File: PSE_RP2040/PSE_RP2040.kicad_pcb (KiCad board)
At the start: 2 copper layers, 100 x 50 mm, 0 parts

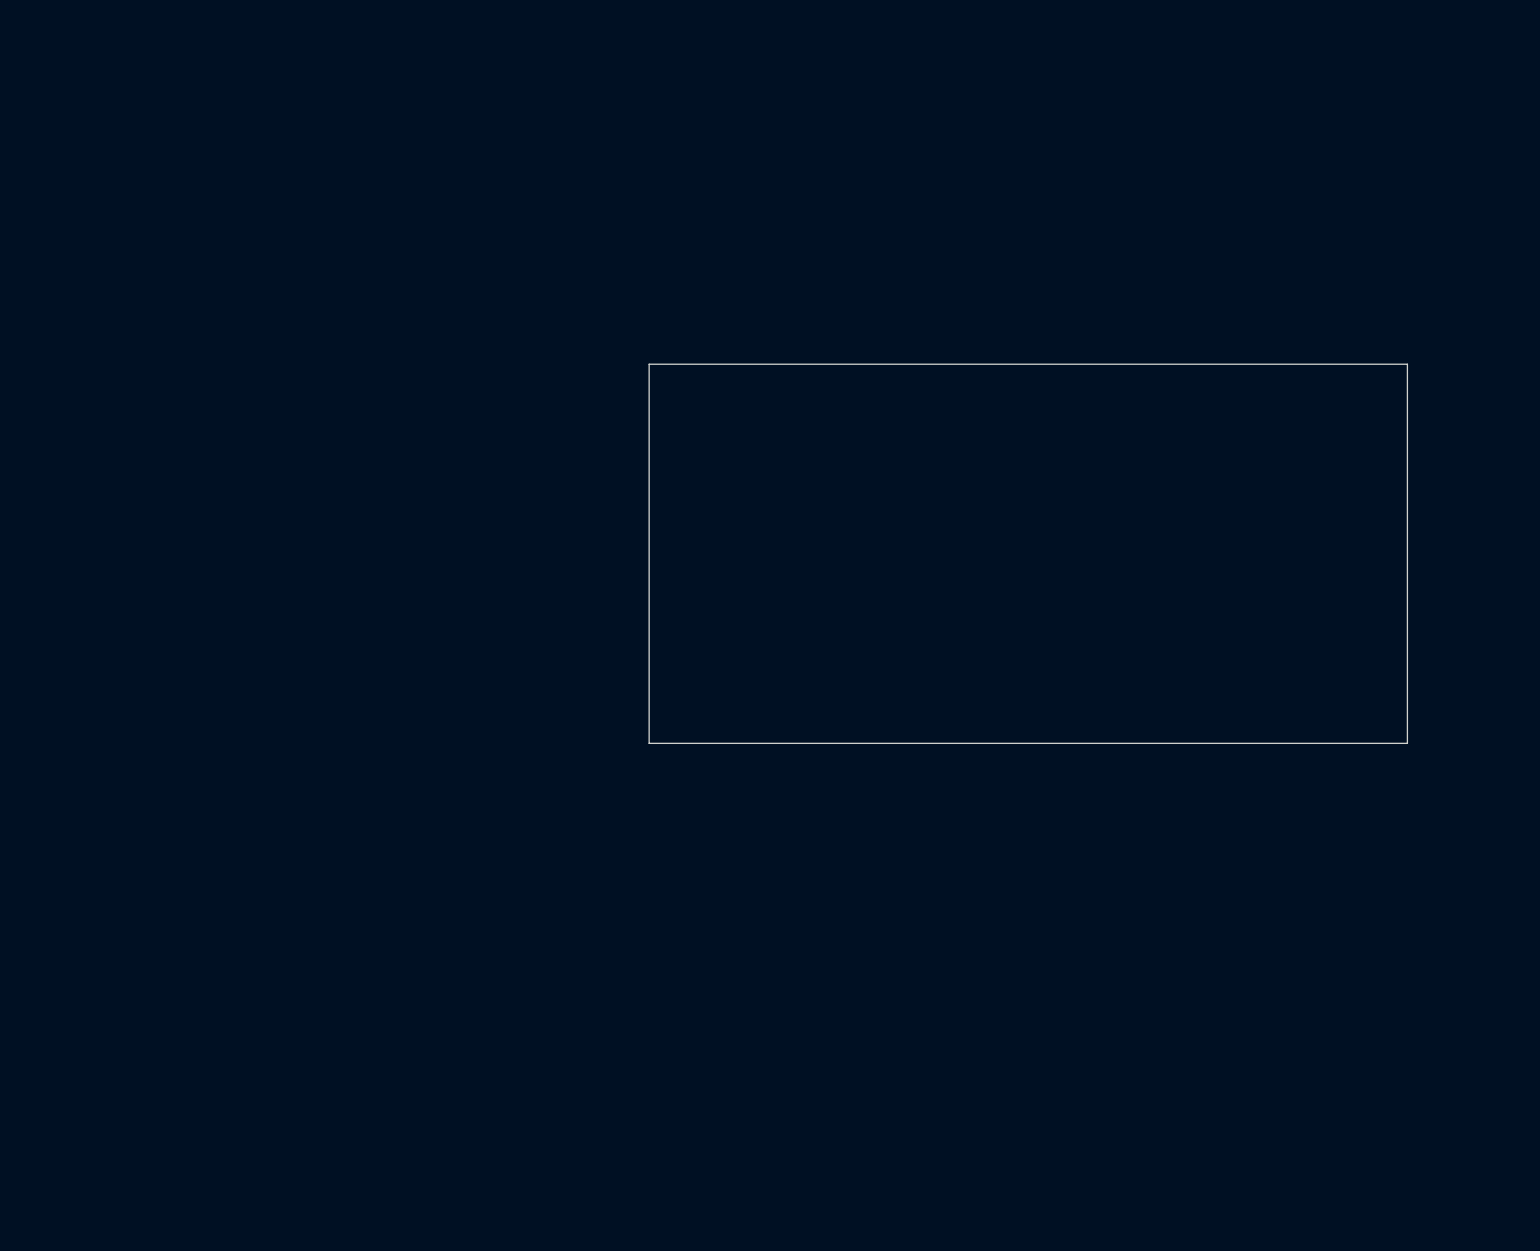
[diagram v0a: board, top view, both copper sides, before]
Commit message: check pin, footprint e symb mem
tolto pin 9 al simbolo memoria
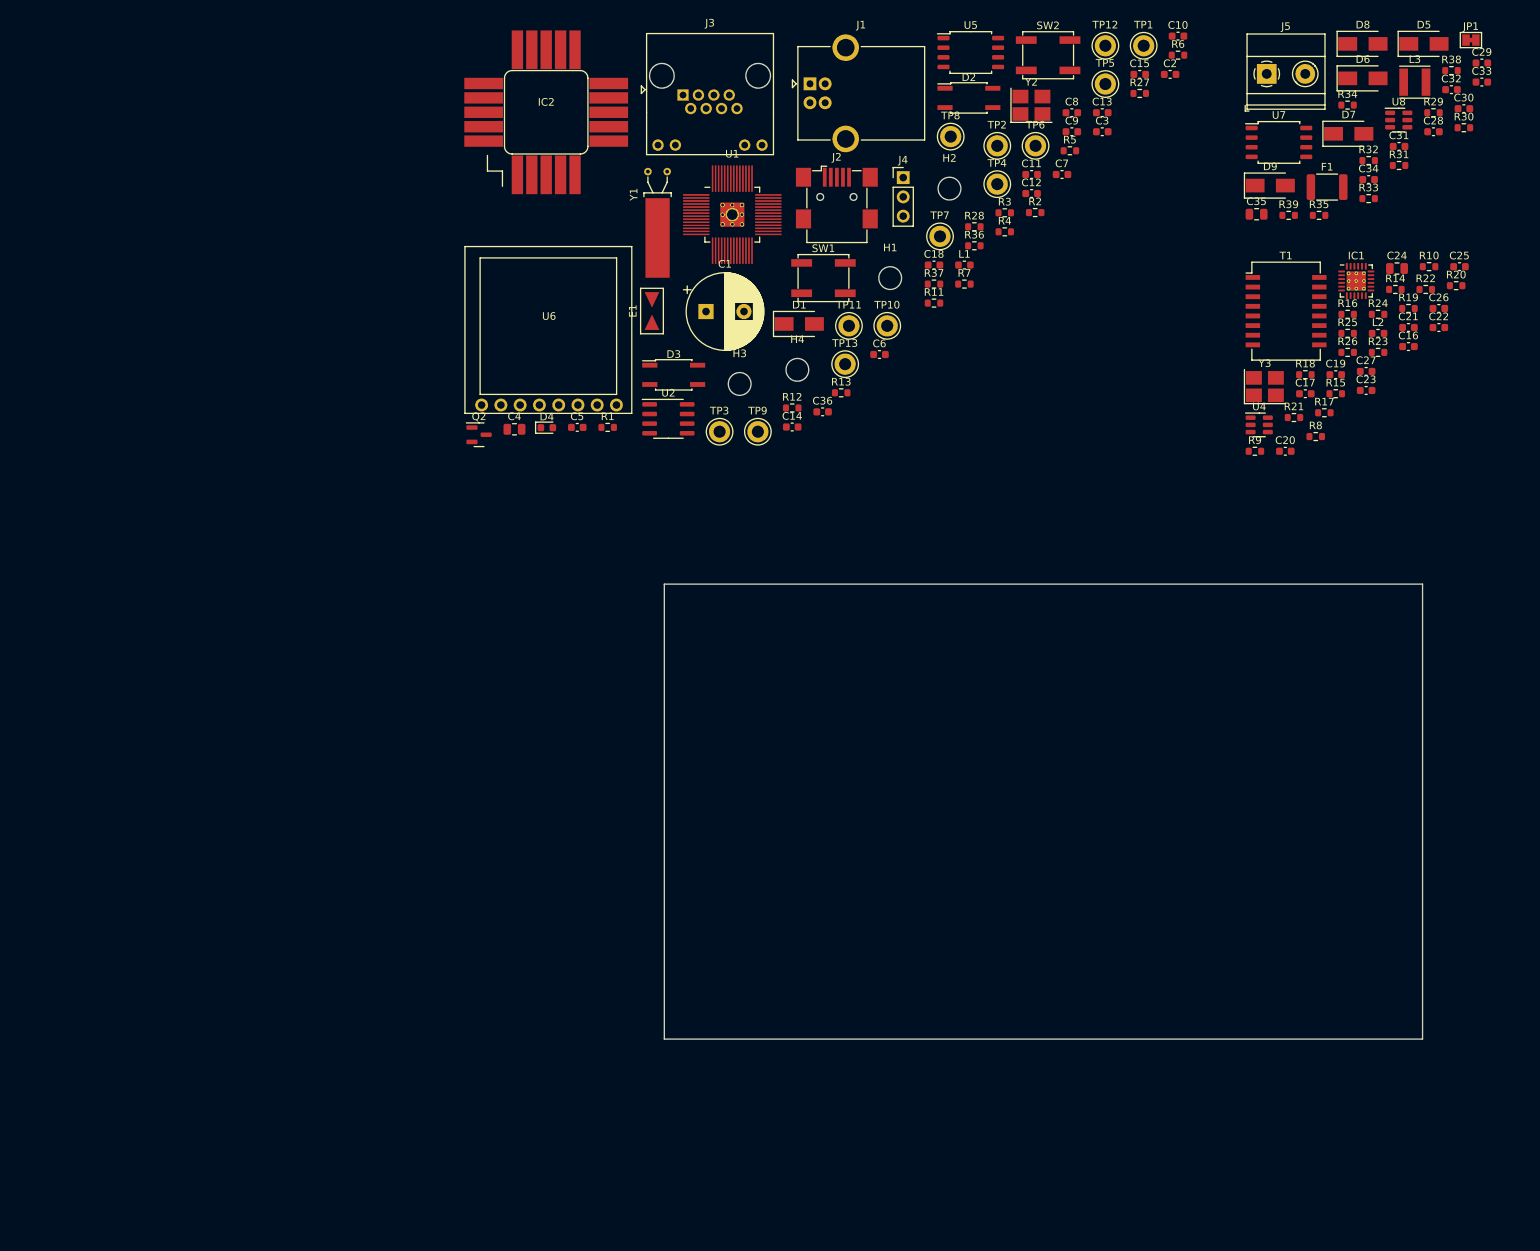
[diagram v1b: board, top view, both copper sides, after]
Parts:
- added C1: 0.1F, Capacitor_THT:CP_Radial_D10.0mm_P5.00mm, F.Cu at (105.5, 64.0)
- added C10: 100n, Capacitor_SMD:C_0603_1608Metric, F.Cu at (167.8, 27.7)
- added C11: 100n, Capacitor_SMD:C_0603_1608Metric, F.Cu at (148.4, 46.0)
- added C12: 2u2, Capacitor_SMD:C_0603_1608Metric, F.Cu at (148.4, 48.5)
- added C13: 100n, Capacitor_SMD:C_0603_1608Metric, F.Cu at (157.8, 37.8)
- added C14: 2u2, Capacitor_SMD:C_0603_1608Metric, F.Cu at (116.9, 79.3)
- added C15: 100n, Capacitor_SMD:C_0603_1608Metric, F.Cu at (162.7, 32.8)
- added C16: 100n, Capacitor_SMD:C_0603_1608Metric, F.Cu at (198.1, 68.7)
- added C17: 1u, Capacitor_SMD:C_0603_1608Metric, F.Cu at (184.5, 74.9)
- added C18: 2u2, Capacitor_SMD:C_0603_1608Metric, F.Cu at (135.6, 57.9)
- added C19: 470p, Capacitor_SMD:C_0603_1608Metric, F.Cu at (188.6, 72.4)
- added C2: 12p, Capacitor_SMD:C_0603_1608Metric, F.Cu at (166.7, 32.8)
- added C20: 12p, Capacitor_SMD:C_0603_1608Metric, F.Cu at (181.9, 82.5)
- added C21: 12p, Capacitor_SMD:C_0603_1608Metric, F.Cu at (198.1, 66.2)
- added C22: 100n, Capacitor_SMD:C_0603_1608Metric, F.Cu at (202.2, 66.2)
- added C23: 100n, Capacitor_SMD:C_0603_1608Metric, F.Cu at (192.6, 74.5)
- added C24: 10u 16V, Capacitor_SMD:C_0805_2012Metric, F.Cu at (196.6, 58.4)
- added C25: 100n, Capacitor_SMD:C_0603_1608Metric, F.Cu at (204.9, 58.1)
- added C26: 100n, Capacitor_SMD:C_0603_1608Metric, F.Cu at (202.2, 63.6)
- added C27: 100n, Capacitor_SMD:C_0603_1608Metric, F.Cu at (192.6, 72.0)
- added C28: 100n 100v, Capacitor_SMD:C_0603_1608Metric, F.Cu at (201.4, 40.3)
- added C29: 2u2, Capacitor_SMD:C_0603_1608Metric, F.Cu at (207.8, 31.3)
- added C3: 100n, Capacitor_SMD:C_0603_1608Metric, F.Cu at (157.8, 40.3)
- added C30: 2u2, Capacitor_SMD:C_0603_1608Metric, F.Cu at (205.4, 37.3)
- added C31: 100n 100v, Capacitor_SMD:C_0603_1608Metric, F.Cu at (196.9, 42.3)
- added C32: 100n, Capacitor_SMD:C_0603_1608Metric, F.Cu at (203.8, 34.8)
- added C33: 470p, Capacitor_SMD:C_0603_1608Metric, F.Cu at (207.8, 33.8)
- added C34: 100n, Capacitor_SMD:C_0603_1608Metric, F.Cu at (192.9, 46.6)
- added C35: 100u, Capacitor_SMD:C_0805_2012Metric, F.Cu at (178.1, 51.2)
- added C36: 10n, Capacitor_SMD:C_0603_1608Metric, F.Cu at (120.9, 77.3)
- added C4: 10u, Capacitor_SMD:C_0805_2012Metric, F.Cu at (80.2, 79.6)
- added C5: 12p, Capacitor_SMD:C_0603_1608Metric, F.Cu at (88.5, 79.3)
- added C6: 100n, Capacitor_SMD:C_0603_1608Metric, F.Cu at (128.4, 69.7)
- added C7: 100n, Capacitor_SMD:C_0603_1608Metric, F.Cu at (152.4, 46.0)
- added C8: 100n, Capacitor_SMD:C_0603_1608Metric, F.Cu at (153.8, 37.8)
- added C9: 100n, Capacitor_SMD:C_0603_1608Metric, F.Cu at (153.8, 40.3)
- added D1: D_Schottky, Diode_SMD:D_SMA, F.Cu at (117.8, 65.7)
- added D2: MB1S, Package_SO:SO-4_4.4x3.6mm_P2.54mm, F.Cu at (140.2, 35.9)
- added D3: MB1S, Package_SO:SO-4_4.4x3.6mm_P2.54mm, F.Cu at (101.2, 72.4)
- added D4: LED, LED_SMD:LED_0603_1608Metric, F.Cu at (84.5, 79.4)
- added D5: S1B, Diode_SMD:D_SMA, F.Cu at (200.2, 28.8)
- added D6: D_Schottky, Diode_SMD:D_SMA, F.Cu at (192.1, 33.3)
- added D7: SMAJ56, Diode_SMD:D_SMA, F.Cu at (190.3, 40.6)
- added D8: S1B, Diode_SMD:D_SMA, F.Cu at (192.1, 28.8)
- added D9: D_Schottky, Diode_SMD:D_SMA, F.Cu at (179.9, 47.4)
- added E1: SparkGap, PSE2021:SPARK_GAP_TRIANGLE, F.Cu at (98.4, 64.0)
- added F1: Polyfuse_Small: fino a 500ma, Fuse:Fuse_1812_4532Metric, F.Cu at (187.4, 47.6)
- added H1: MountingHole, MountingHole:MountingHole_3mm, F.Cu at (129.8, 59.6)
- added H2: MountingHole, MountingHole:MountingHole_3mm, F.Cu at (137.6, 47.8)
- added H3: MountingHole, MountingHole:MountingHole_3mm, F.Cu at (109.9, 73.6)
- added H4: MountingHole, MountingHole:MountingHole_3mm, F.Cu at (117.5, 71.7)
- added IC1: LAN8742A-CZ, Package_DFN_QFN:HVQFN-24-1EP_4x4mm_P0.5mm_EP2.5x2.5mm_ThermalVias, F.Cu at (191.3, 60.0)
- added IC2: SAM-M8Q-0, PSE2021:SAM-M8Q, F.Cu at (84.4, 37.8)
- added J1: USB_B, Connector_USB:USB_B_OST_USB-B1HSxx_Horizontal, F.Cu at (119.2, 34.0)
- added J2: USB_B_Mini, Connector_USB:USB_Mini-B_Wuerth_65100516121_Horizontal, F.Cu at (122.8, 48.9)
- added J3: 8P8C_LED, PSE2021:RJ45_Amphenol_RJHSE-5081, F.Cu at (102.5, 35.5)
- added J4: Conn_01x03, Connector_PinHeader_2.54mm:PinHeader_1x03_P2.54mm_Vertical, F.Cu at (131.5, 46.4)
- added J5: Screw_Terminal_01x02, TerminalBlock_Phoenix:TerminalBlock_Phoenix_MKDS-1,5-2-5.08_1x02_P5.08mm_Horizontal, F.Cu at (179.4, 32.7)
- added JP1: SolderJumper_2_Bridged, Jumper:SolderJumper-2_P1.3mm_Bridged_Pad1.0x1.5mm, F.Cu at (206.4, 28.2)
- added L1: 200mA 120Ohm, Inductor_SMD:L_0603_1608Metric, F.Cu at (139.6, 57.9)
- added L2: 25uH, Inductor_SMD:L_0603_1608Metric, F.Cu at (194.1, 66.9)
- added L3: 22u, Inductor_SMD:L_Vishay_IFSC-1515AH_4x4x1.8mm, F.Cu at (199.0, 33.8)
- added Q2: IRLML6402, Package_TO_SOT_SMD:SOT-23, F.Cu at (75.6, 80.3)
- added R1: 1k, Resistor_SMD:R_0603_1608Metric, F.Cu at (92.5, 79.3)
- added R10: 10k, Resistor_SMD:R_0603_1608Metric, F.Cu at (200.9, 58.1)
- added R11: 1k, Resistor_SMD:R_0603_1608Metric, F.Cu at (135.6, 62.9)
- added R12: 27, Resistor_SMD:R_0603_1608Metric, F.Cu at (116.9, 76.8)
- added R13: 27, Resistor_SMD:R_0603_1608Metric, F.Cu at (123.3, 74.8)
- added R14: 10k, Resistor_SMD:R_0603_1608Metric, F.Cu at (196.4, 61.1)
- added R15: 10k, Resistor_SMD:R_0603_1608Metric, F.Cu at (188.6, 74.9)
- added R16: 33, Resistor_SMD:R_0603_1608Metric, F.Cu at (190.1, 64.4)
- added R17: 10k, Resistor_SMD:R_0603_1608Metric, F.Cu at (187.1, 77.4)
- added R18: 10k, Resistor_SMD:R_0603_1608Metric, F.Cu at (184.5, 72.4)
- added R19: 10k, Resistor_SMD:R_0603_1608Metric, F.Cu at (198.1, 63.6)
- added R2: 100, Resistor_SMD:R_0603_1608Metric, F.Cu at (148.9, 51.0)
- added R20: 10k, Resistor_SMD:R_0603_1608Metric, F.Cu at (204.4, 60.6)
- added R21: 10k, Resistor_SMD:R_0603_1608Metric, F.Cu at (183.0, 78.0)
- added R22: 12k1, Resistor_SMD:R_0603_1608Metric, F.Cu at (200.4, 61.1)
- added R23: 49,9, Resistor_SMD:R_0603_1608Metric, F.Cu at (194.1, 69.4)
- added R24: 49,9, Resistor_SMD:R_0603_1608Metric, F.Cu at (194.1, 64.4)
- added R25: 49,9, Resistor_SMD:R_0603_1608Metric, F.Cu at (190.1, 66.9)
- added R26: 49,9, Resistor_SMD:R_0603_1608Metric, F.Cu at (190.1, 69.4)
- added R27: 47k, Resistor_SMD:R_0603_1608Metric, F.Cu at (162.7, 35.3)
- added R28: R4 no fit (o 10k), Resistor_SMD:R_0603_1608Metric, F.Cu at (140.9, 52.9)
- added R29: 50k, Resistor_SMD:R_0603_1608Metric, F.Cu at (201.4, 37.8)
- added R3: R, Resistor_SMD:R_0603_1608Metric, F.Cu at (144.9, 51.0)
- added R30: 178k, Resistor_SMD:R_0603_1608Metric, F.Cu at (205.4, 39.8)
- added R31: 50k, Resistor_SMD:R_0603_1608Metric, F.Cu at (196.9, 44.8)
- added R32: 330, Resistor_SMD:R_0603_1608Metric, F.Cu at (192.9, 44.1)
- added R33: 27, Resistor_SMD:R_0603_1608Metric, F.Cu at (192.9, 49.2)
- added R34: 33k, Resistor_SMD:R_0603_1608Metric, F.Cu at (190.1, 36.8)
- added R35: 10k, Resistor_SMD:R_0603_1608Metric, F.Cu at (186.3, 51.4)
- added R36: 1M, Resistor_SMD:R_0603_1608Metric, F.Cu at (140.9, 55.4)
- added R37: 1k, Resistor_SMD:R_0603_1608Metric, F.Cu at (135.6, 60.4)
- added R38: 0R NF, Resistor_SMD:R_0603_1608Metric, F.Cu at (203.8, 32.3)
- added R39: 0R NF, Resistor_SMD:R_0603_1608Metric, F.Cu at (182.3, 51.4)
- added R4: 10k, Resistor_SMD:R_0603_1608Metric, F.Cu at (144.9, 53.5)
- added R5: 10k, Resistor_SMD:R_0603_1608Metric, F.Cu at (153.5, 42.9)
- added R6: 270, Resistor_SMD:R_0603_1608Metric, F.Cu at (167.8, 30.2)
- added R7: 270, Resistor_SMD:R_0603_1608Metric, F.Cu at (139.6, 60.4)
- added R8: 33, Resistor_SMD:R_0603_1608Metric, F.Cu at (185.9, 80.5)
- added R9: 33, Resistor_SMD:R_0603_1608Metric, F.Cu at (177.9, 82.5)
- added SW1: SW_Push, Button_Switch_SMD:SW_SPST_EVQP0, F.Cu at (121.0, 59.6)
- added SW2: SW_Push, Button_Switch_SMD:SW_SPST_EVQP0, F.Cu at (150.6, 30.2)
- added T1: 749013011, Transformer_SMD:Transformer_Ethernet_Wuerth_749013011A, F.Cu at (182.0, 64.0)
- added TP1: 3V3, TestPoint:TestPoint_Keystone_5005-5009_Compact, F.Cu at (163.2, 29.0)
- added TP10: UART_RX-GPS_TX, TestPoint:TestPoint_Keystone_5005-5009_Compact, F.Cu at (129.4, 65.9)
- added TP11: VCC_GPS, TestPoint:TestPoint_Keystone_5005-5009_Compact, F.Cu at (124.3, 65.9)
- added TP12: I2C_SCL_RTC, TestPoint:TestPoint_Keystone_5005-5009_Compact, F.Cu at (158.2, 29.0)
- added TP13: I2C_SDA_RTC, TestPoint:TestPoint_Keystone_5005-5009_Compact, F.Cu at (123.8, 71.0)
- added TP2: GND, TestPoint:TestPoint_Keystone_5005-5009_Compact, F.Cu at (143.9, 42.2)
- added TP3: 5V, TestPoint:TestPoint_Keystone_5005-5009_Compact, F.Cu at (107.3, 79.9)
- added TP4: 1V1, TestPoint:TestPoint_Keystone_5005-5009_Compact, F.Cu at (143.9, 47.2)
- added TP5: POE+, TestPoint:TestPoint_Keystone_5005-5009_Compact, F.Cu at (158.2, 34.0)
- added TP6: POE-, TestPoint:TestPoint_Keystone_5005-5009_Compact, F.Cu at (149.0, 42.2)
- added TP7: USB_DP, TestPoint:TestPoint_Keystone_5005-5009_Compact, F.Cu at (136.4, 54.1)
- added TP8: USB_DN, TestPoint:TestPoint_Keystone_5005-5009_Compact, F.Cu at (137.8, 41.0)
- added TP9: UART_TX-GPS_RX, TestPoint:TestPoint_Keystone_5005-5009_Compact, F.Cu at (112.3, 79.9)
- added U1: RP2040, PSE2021:RP2040-QFN-56, F.Cu at (109.0, 51.3)
- added U2: PCF8563T, Package_SO:SOIC-8_3.9x4.9mm_P1.27mm, F.Cu at (100.5, 78.2)
- added U4: USBLC6-4SC6, Package_TO_SOT_SMD:SOT-23-6, F.Cu at (178.5, 79.0)
- added U5: W25Q16JVUSSQ, Package_SO:SOIC-8_5.275x5.275mm_P1.27mm, F.Cu at (140.4, 29.9)
- added U6: PAM7Q, PSE2021:PAM-7Q, F.Cu at (84.7, 66.5)
- added U7: TPS2375-1, Package_SO:SOIC-8_5.275x5.275mm_P1.27mm, F.Cu at (181.1, 41.8)
- added U8: LMR16006YQ, Package_TO_SOT_SMD:SOT-23-6, F.Cu at (196.9, 38.8)
- added Y1: Crystal_GND3, Crystal:Crystal_AT310_D3.0mm_L10.0mm_Horizontal_1EP_style1, F.Cu at (97.8, 45.6)
- added Y2: Crystal_GND24, Crystal:Crystal_SMD_3225-4Pin_3.2x2.5mm_HandSoldering, F.Cu at (148.4, 36.9)
- added Y3: 25MHz, Crystal:Crystal_SMD_3225-4Pin_3.2x2.5mm_HandSoldering, F.Cu at (179.2, 74.0)
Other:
- board size 100 x 50 mm -> 100 x 60 mm

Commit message: piazzamento componenti pcb 1
piazzamento di massima
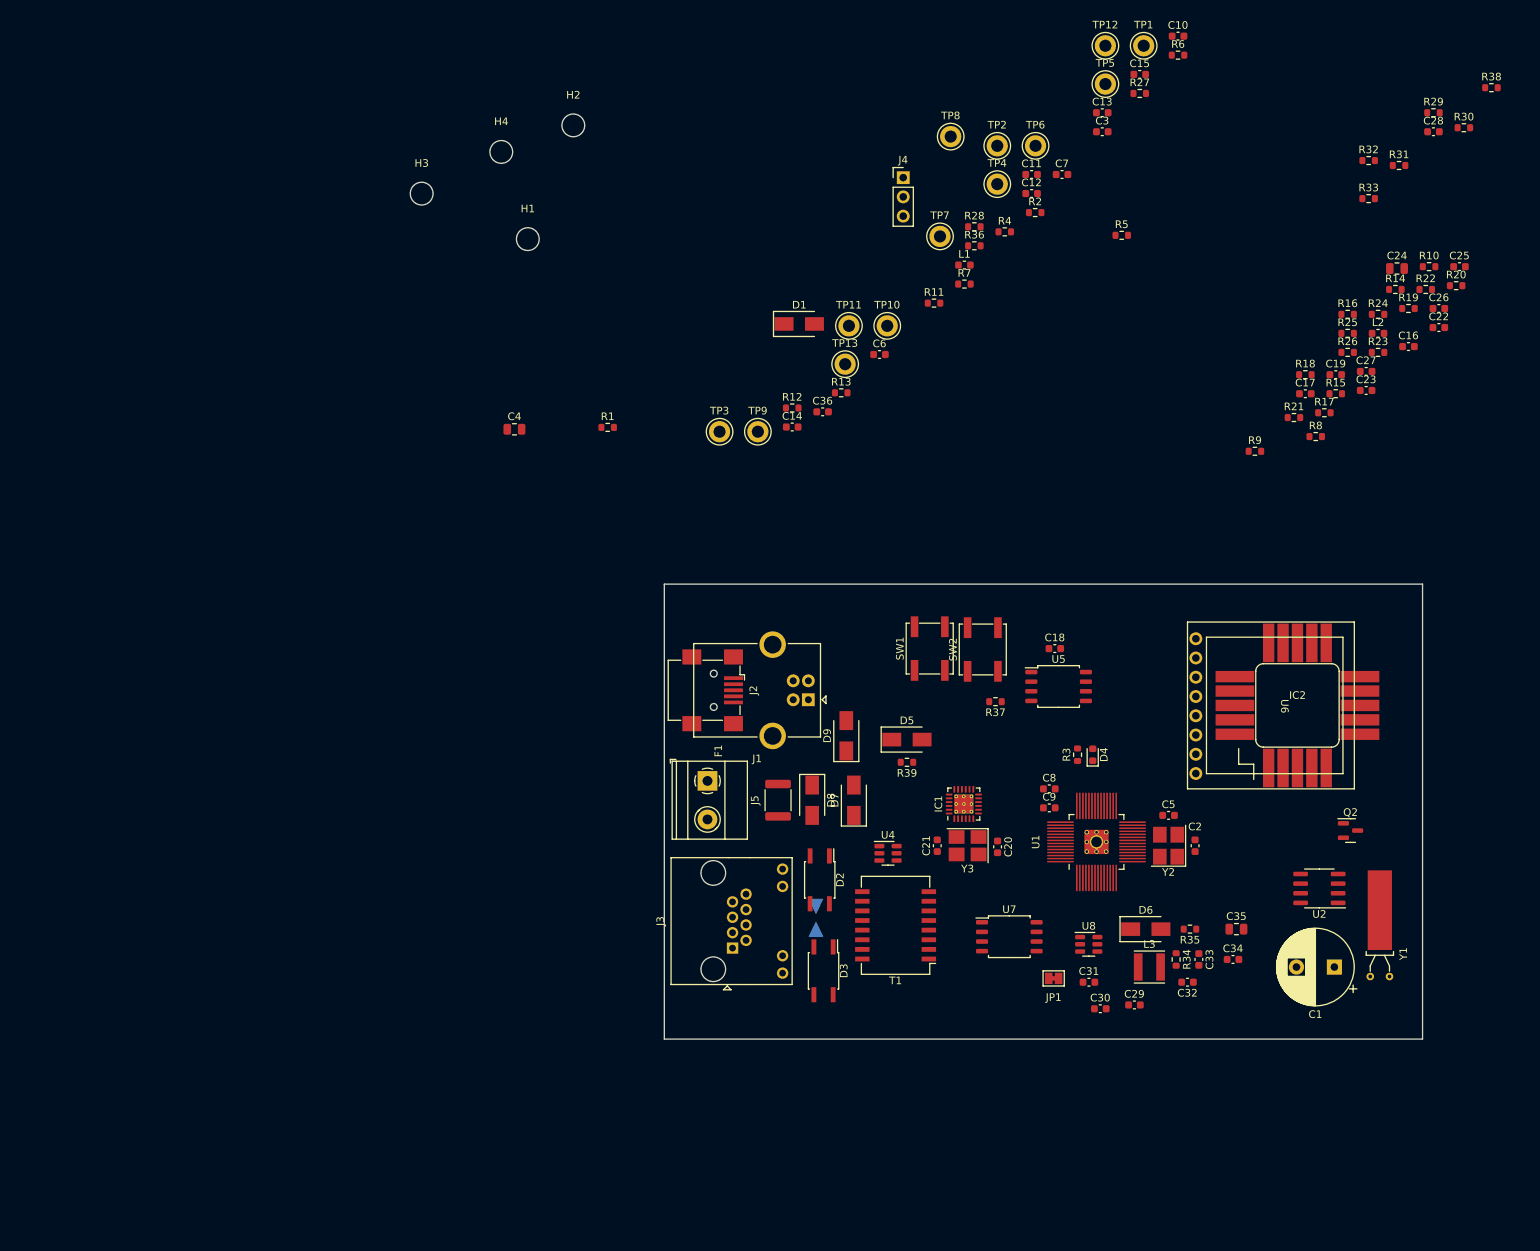
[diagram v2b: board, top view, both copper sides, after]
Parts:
- E1: moved to B.Cu
- moved Y1 144.3 mm to (195.6, 151.8), turned to 180 degrees
- moved JP1 135.4 mm to (151.3, 152.0)
- moved C29 132.4 mm to (162.0, 155.5)
- moved C30 128.0 mm to (157.5, 156.0)
- moved IC2 126.2 mm to (183.5, 116.0)
- moved Q2 126.2 mm to (190.5, 132.5)
- moved D8 123.4 mm to (119.5, 128.5), turned to -90 degrees
- moved C32 122.7 mm to (169.0, 152.5), turned to 180 degrees
- moved L3 121.8 mm to (164.0, 150.5)
- moved C33 121.6 mm to (170.5, 149.5), turned to -90 degrees
- moved C1 119.7 mm to (188.4, 150.5), turned to 180 degrees
- moved J5 118.9 mm to (105.7, 126.0), turned to -90 degrees
- moved C31 117.6 mm to (156.0, 152.5)
- moved U8 116.1 mm to (156.0, 147.5)
- moved D6 115.8 mm to (163.5, 145.5)
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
